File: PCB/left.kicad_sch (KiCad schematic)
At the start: 35 parts, among them SW56 SW_Push, SW57 SW_Push, SW58 SW_Push, SW59 SW_Push, SW60 SW_Push, SW61 SW_Push, SW62 SW_Push, SW63 SW_Push, SW64 SW_Push, SW65 SW_Push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

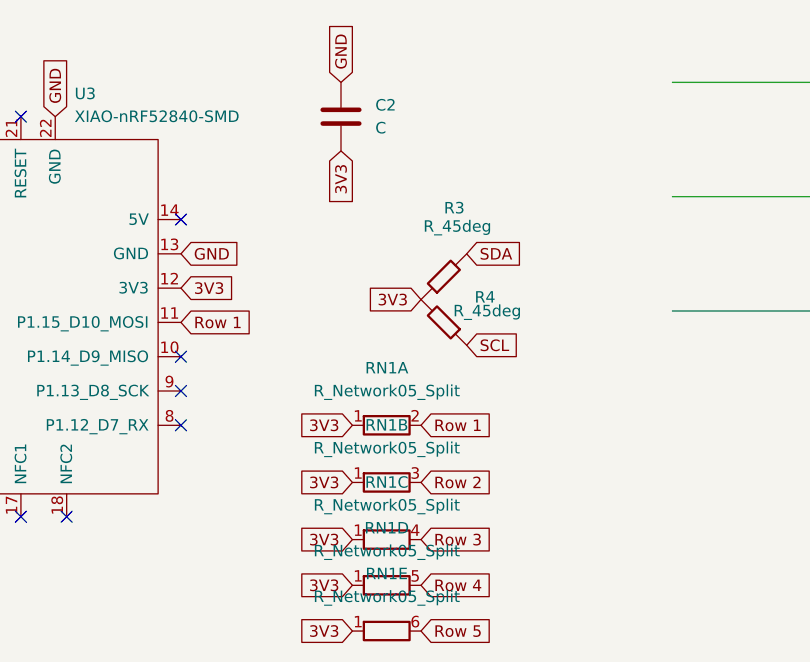
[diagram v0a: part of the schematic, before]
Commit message: Added all files required for the display based keyboard
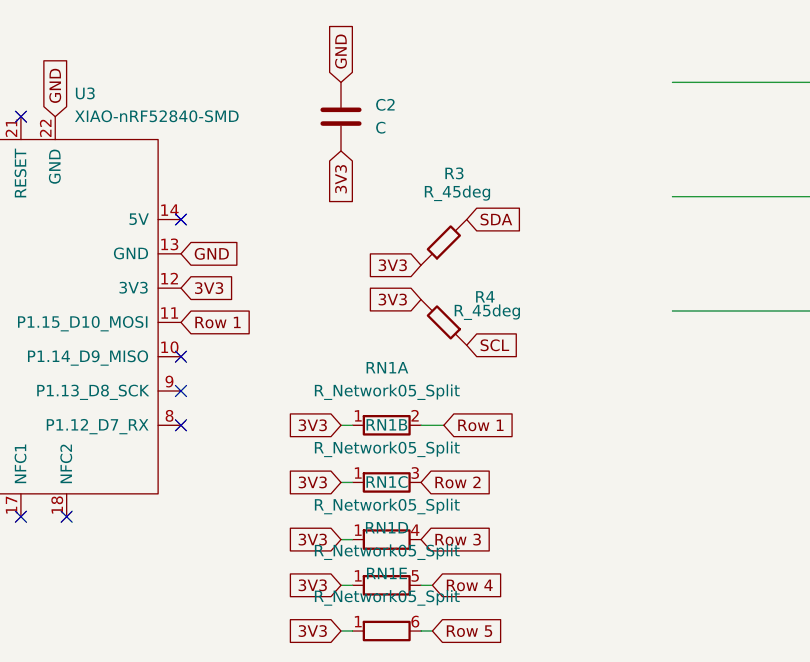
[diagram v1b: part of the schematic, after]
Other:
- moved on the sheet: R3
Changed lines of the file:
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@@
+	(wire
+		(pts
+			(xy 105.41 114.3) (xy 102.87 114.3)
+		)
+		(stroke
+			(width 0)
+			(type default)
+		)
+	)
 	(wire
 		(pts
@@
 	(wire
 		(pts
+			(xy 93.98 137.16) (xy 95.25 137.16)
+		)
+		(stroke
+			(width 0)
+			(type default)
+		)
+	)
+	(wire
+		(pts
+			(xy 93.98 127) (xy 95.25 127)
+		)
+		(stroke
+			(width 0)
+			(type default)
+		)
+	)
+	(wire
+		(pts
 			(xy 196.85 68.58) (xy 196.85 81.28)
 		)
@@
 	(wire
 		(pts
+			(xy 93.98 132.08) (xy 95.25 132.08)
+		)
+		(stroke
+			(width 0)
+			(type default)
+		)
+	)
+	(wire
+		(pts
+			(xy 93.98 120.65) (xy 95.25 120.65)
+		)
+		(stroke
+			(width 0)
+			(type default)
+		)
+	)
+	(wire
+		(pts
 			(xy 194.31 63.5) (xy 207.01 63.5)
 		)
@@
 	(wire
 		(pts
+			(xy 104.14 137.16) (xy 102.87 137.16)
+		)
+		(stroke
+			(width 0)
+			(type default)
+		)
+	)
+	(wire
+		(pts
 			(xy 194.31 88.9) (xy 207.01 88.9)
 		)
@@
 	(wire
 		(pts
+			(xy 104.14 132.08) (xy 102.87 132.08)
+		)
+		(stroke
+			(width 0)
+			(type default)
+		)
+	)
+	(wire
+		(pts
 			(xy 196.85 93.98) (xy 196.85 107.95)
 		)
@@
 	(wire
 		(pts
+			(xy 93.98 114.3) (xy 95.25 114.3)
+		)
+		(stroke
+			(width 0)
+			(type default)
+		)
+	)
+	(wire
+		(pts
 			(xy 219.71 50.8) (xy 222.25 50.8)
 		)
@@
 	(global_label "3V3"
 		(shape input)
+		(at 102.87 100.33 180)
+		(fields_autoplaced yes)
+		(effects
+			(font
+				(size 1.27 1.27)
+			)
+			(justify right)
+		)
+		(property "Intersheetrefs" "${INTERSHEET_REFS}"
+			(at 96.3772 100.33 0)
+			(effects
+				(font
+					(size 1.27 1.27)
+				)
+				(justify right)
+				(hide yes)
+			)
+		)
+	)
+	(global_label "3V3"
+		(shape input)
 		(at 93.98 83.82 270)
 		(fields_autoplaced yes)
@@
 	(global_label "3V3"
 		(shape input)
-		(at 95.25 132.08 180)
+		(at 93.98 132.08 180)
 		(fields_autoplaced yes)
 		(effects
@@
 		)
 		(property "Intersheetrefs" "${INTERSHEET_REFS}"
-			(at 88.7572 132.08 0)
+			(at 87.4872 132.08 0)
 			(effects
 				(font
@@
 	(global_label "Row 4"
 		(shape input)
-		(at 102.87 132.08 0)
-		(fields_autoplaced yes)
-		(effects
-			(font
-				(size 1.27 1.27)
-			)
-			(justify left)
-		)
-		(property "Intersheetrefs" "${INTERSHEET_REFS}"
-			(at 111.7818 132.08 0)
+		(at 104.14 132.08 0)
+		(fields_autoplaced yes)
+		(effects
+			(font
+				(size 1.27 1.27)
+			)
+			(justify left)
+		)
+		(property "Intersheetrefs" "${INTERSHEET_REFS}"
+			(at 113.0518 132.08 0)
 			(effects
 				(font
@@
 	(global_label "Row 1"
 		(shape input)
-		(at 102.87 114.3 0)
-		(fields_autoplaced yes)
-		(effects
-			(font
-				(size 1.27 1.27)
-			)
-			(justify left)
-		)
-		(property "Intersheetrefs" "${INTERSHEET_REFS}"
-			(at 111.7818 114.3 0)
+		(at 105.41 114.3 0)
+		(fields_autoplaced yes)
+		(effects
+			(font
+				(size 1.27 1.27)
+			)
+			(justify left)
+		)
+		(property "Intersheetrefs" "${INTERSHEET_REFS}"
+			(at 114.3218 114.3 0)
 			(effects
 				(font
@@
 	(global_label "Row 5"
 		(shape input)
-		(at 102.87 137.16 0)
-		(fields_autoplaced yes)
-		(effects
-			(font
-				(size 1.27 1.27)
-			)
-			(justify left)
-		)
-		(property "Intersheetrefs" "${INTERSHEET_REFS}"
-			(at 111.7818 137.16 0)
+		(at 104.14 137.16 0)
+		(fields_autoplaced yes)
+		(effects
+			(font
+				(size 1.27 1.27)
+			)
+			(justify left)
+		)
+		(property "Intersheetrefs" "${INTERSHEET_REFS}"
+			(at 113.0518 137.16 0)
 			(effects
 				(font
@@
 	(global_label "3V3"
 		(shape input)
-		(at 95.25 127 180)
+		(at 102.87 96.52 180)
 		(fields_autoplaced yes)
 		(effects
@@
 		)
 		(property "Intersheetrefs" "${INTERSHEET_REFS}"
-			(at 88.7572 127 0)
+			(at 96.3772 96.52 0)
 			(effects
 				(font
@@
 	(global_label "3V3"
 		(shape input)
-		(at 95.25 114.3 180)
+		(at 93.98 127 180)
 		(fields_autoplaced yes)
 		(effects
@@
 		)
 		(property "Intersheetrefs" "${INTERSHEET_REFS}"
-			(at 88.7572 114.3 0)
+			(at 87.4872 127 0)
+			(effects
+				(font
+					(size 1.27 1.27)
+				)
+				(justify right)
+				(hide yes)
+			)
+		)
+	)
+	(global_label "3V3"
+		(shape input)
+		(at 93.98 114.3 180)
+		(fields_autoplaced yes)
+		(effects
+			(font
+				(size 1.27 1.27)
+			)
+			(justify right)
+		)
+		(property "Intersheetrefs" "${INTERSHEET_REFS}"
+			(at 87.4872 114.3 0)
 			(effects
 				(font
@@
 	(global_label "3V3"
 		(shape input)
-		(at 95.25 137.16 180)
+		(at 93.98 137.16 180)
 		(fields_autoplaced yes)
 		(effects
@@
 		)
 		(property "Intersheetrefs" "${INTERSHEET_REFS}"
-			(at 88.7572 137.16 0)
+			(at 87.4872 137.16 0)
 			(effects
 				(font
@@
 	(global_label "SDA"
 		(shape input)
-		(at 107.95 95.25 0)
-		(fields_autoplaced yes)
-		(effects
-			(font
-				(size 1.27 1.27)
-			)
-			(justify left)
-		)
-		(property "Intersheetrefs" "${INTERSHEET_REFS}"
-			(at 114.5033 95.25 0)
+		(at 107.95 91.44 0)
+		(fields_autoplaced yes)
+		(effects
+			(font
+				(size 1.27 1.27)
+			)
+			(justify left)
+		)
+		(property "Intersheetrefs" "${INTERSHEET_REFS}"
+			(at 114.5033 91.44 0)
 			(effects
 				(font
@@
 	(global_label "3V3"
 		(shape input)
-		(at 102.87 100.33 180)
+		(at 93.98 120.65 180)
 		(fields_autoplaced yes)
 		(effects
@@
 		)
 		(property "Intersheetrefs" "${INTERSHEET_REFS}"
-			(at 96.3772 100.33 0)
-			(effects
-				(font
-					(size 1.27 1.27)
-				)
-				(justify right)
-				(hide yes)
-			)
-		)
-	)
-	(global_label "3V3"
-		(shape input)
-		(at 95.25 120.65 180)
-		(fields_autoplaced yes)
-		(effects
-			(font
-				(size 1.27 1.27)
-			)
-			(justify right)
-		)
-		(property "Intersheetrefs" "${INTERSHEET_REFS}"
-			(at 88.7572 120.65 0)
+			(at 87.4872 120.65 0)
 			(effects
 				(font
@@
 	(symbol
 		(lib_id "Device:R_45deg")
-		(at 105.41 97.79 90)
+		(at 105.41 93.98 90)
 		(unit 1)
 		(exclude_from_sim no)
@@
 		(dnp no)
 		(property "Reference" "R3"
-			(at 105.41 90.17 90)
+			(at 105.41 86.36 90)
 			(effects
 				(font
@@
 		)
 		(property "Value" "R_45deg"
-			(at 103.124 92.202 90)
+			(at 103.124 88.392 90)
 			(effects
 				(font
@@
 		)
 		(property "Footprint" "Resistor_SMD:R_0805_2012Metric_Pad1.20x1.40mm_HandSolder"
-			(at 107.188 97.79 0)
+			(at 107.188 93.98 0)
 			(effects
 				(font
@@
 		)
 		(property "Datasheet" "~"
-			(at 105.41 97.79 0)
+			(at 105.41 93.98 0)
 			(effects
 				(font
@@
 		)
 		(property "Description" "Resistor, rotated by 45°"
-			(at 105.41 97.79 0)
-			(effects
-				(font
+			(at 105.41 93.98 0)
+			(effects
+				(font
